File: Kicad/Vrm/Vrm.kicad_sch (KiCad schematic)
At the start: 28 parts, among them J1 Screw_Terminal_01x05, J2 AVR-JTAG-10, J3 Screw_Terminal_01x03, J4 Screw_Terminal_01x04, Q1 FMMT458TA - SOT23, SW1 Switch, U1 STM32F091RCTx

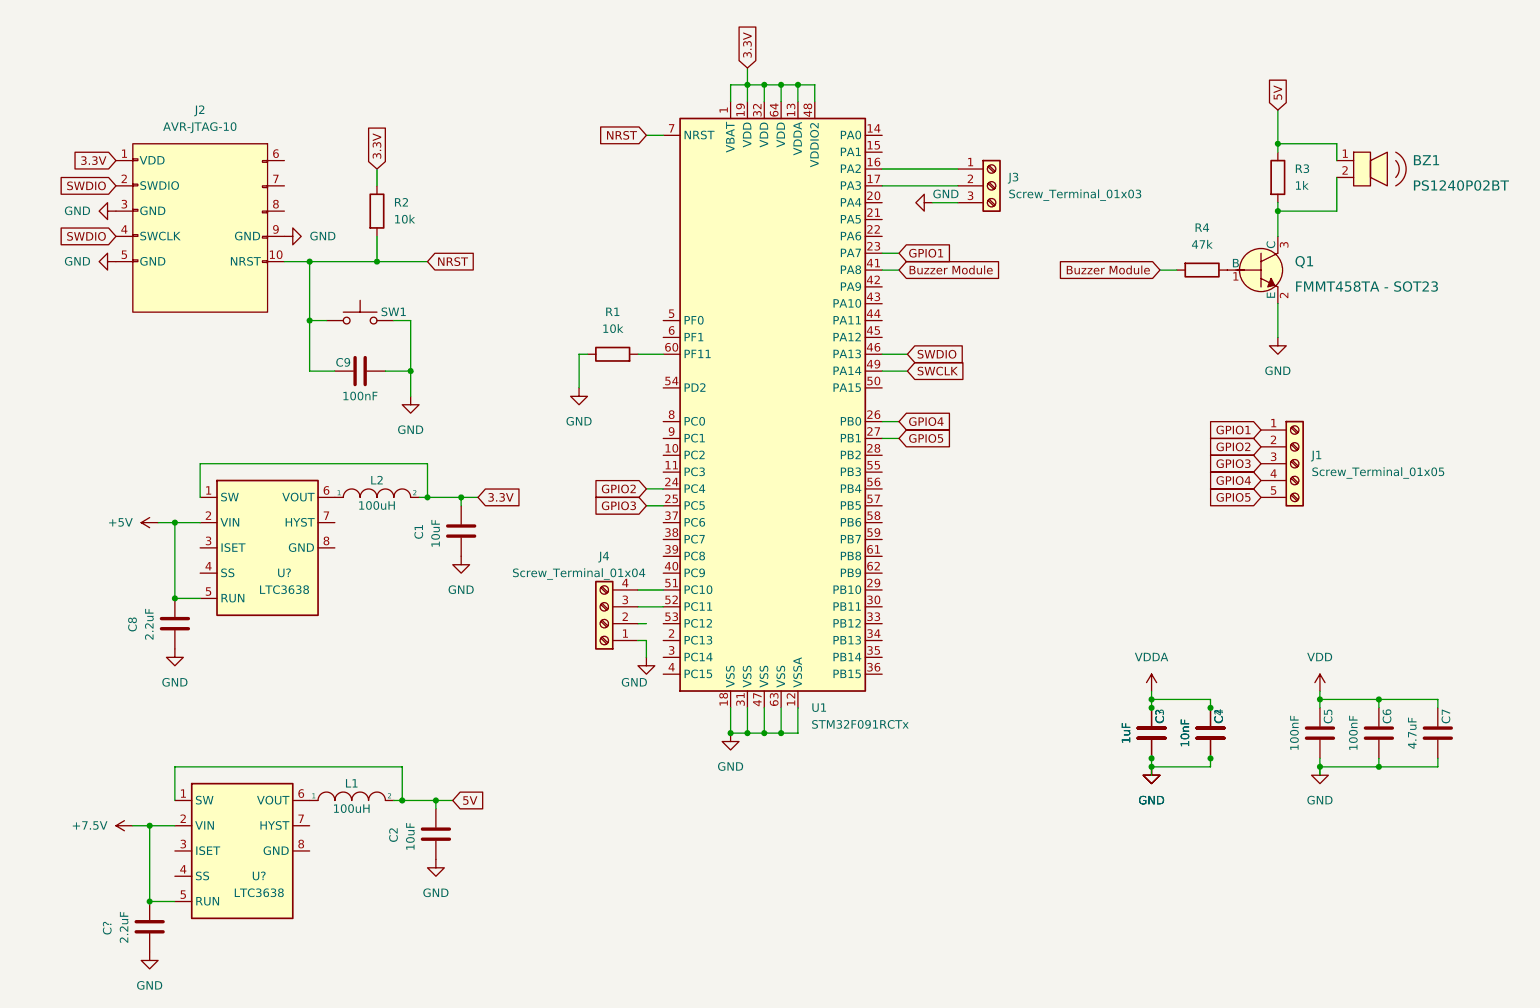
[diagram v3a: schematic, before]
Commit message: Added UART resistors, new buzzer, UART breakout, and ground plane
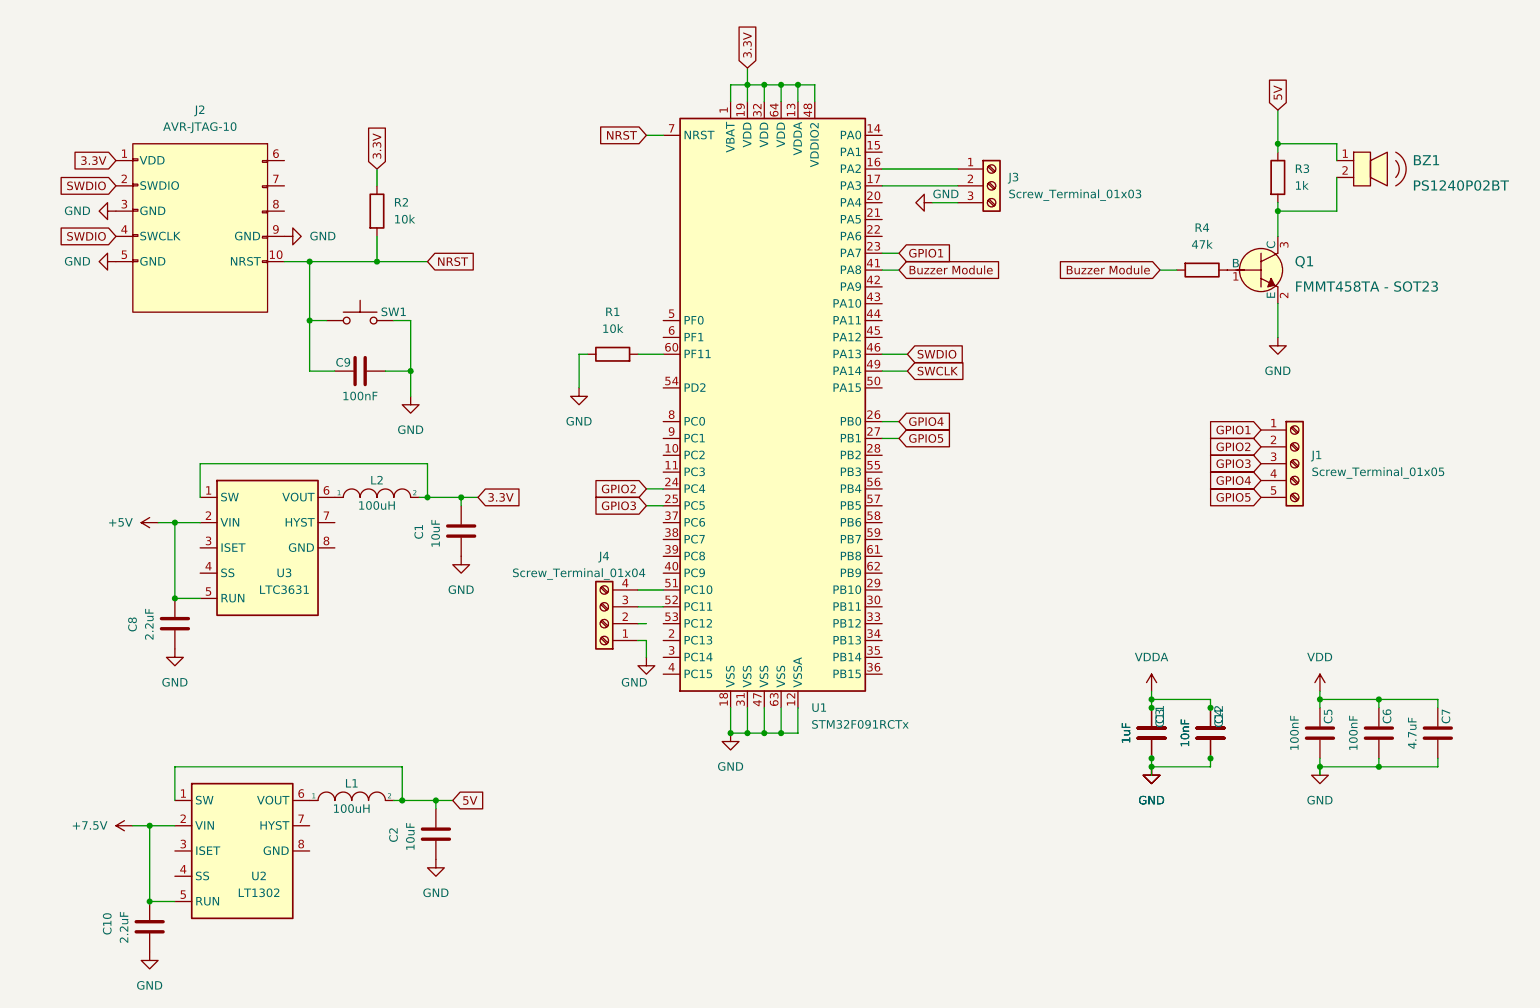
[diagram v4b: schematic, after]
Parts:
- U2: renamed from U?; value LTC3638 -> LT1302
- U3: renamed from U?; value LTC3638 -> LTC3631
- gave numbers to parts that had none: 3
